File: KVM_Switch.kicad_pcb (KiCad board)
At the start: 4 copper layers, 100 x 70 mm, 110 parts, among them J1 HDMI_A, J2 HDMI_A, J3 HDMI_A, J4 USB_C_Receptacle_USB2.0_16P, J5 USB_C_Receptacle_USB2.0_16P, J6 USB_C_Receptacle_USB2.0_16P, J7 USB_A_Stacked, J8 USB_A_Stacked, SW1 SPST-NO, U1 TPD4E02B04DQA, U10 USBLC6-2SC6, U11 TS3USB221AQRSERQ1, U12 USBLC6-2SC6, U13 USB2514B_Bi, U14 USBLC6-2SC6, U15 USBLC6-2SC6, U16 USBLC6-2SC6, U17 USBLC6-2SC6, U2 TPD4E02B04DQA, U3 TPD4E02B04DQA, U4 TPD4E02B04DQA, U5 HD3SS215RTQR, U6 TPD4E02B04DQA, U7 TPD4E02B04DQA, U8 TLV75533PDBV, U9 STM32C031G6Ux, X1 24MHz

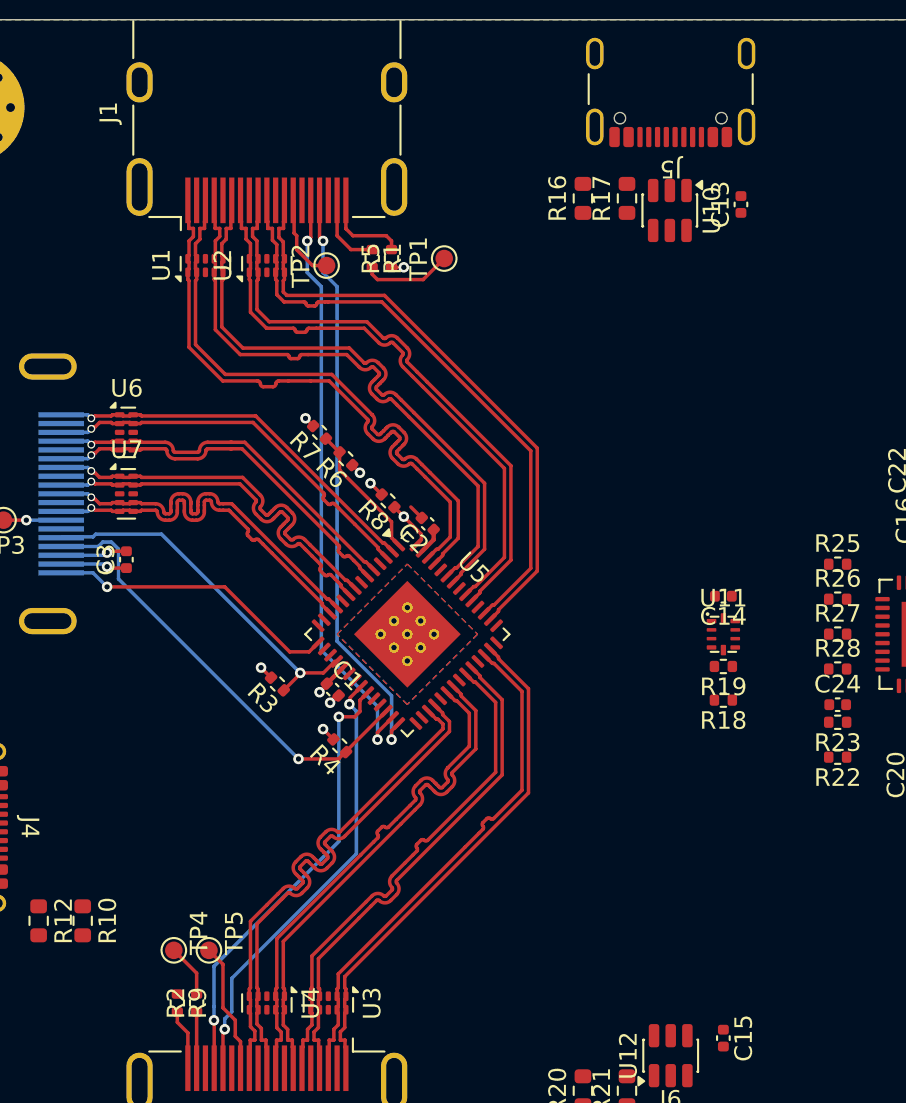
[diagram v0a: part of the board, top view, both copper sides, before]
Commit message: TMDS tunned to length
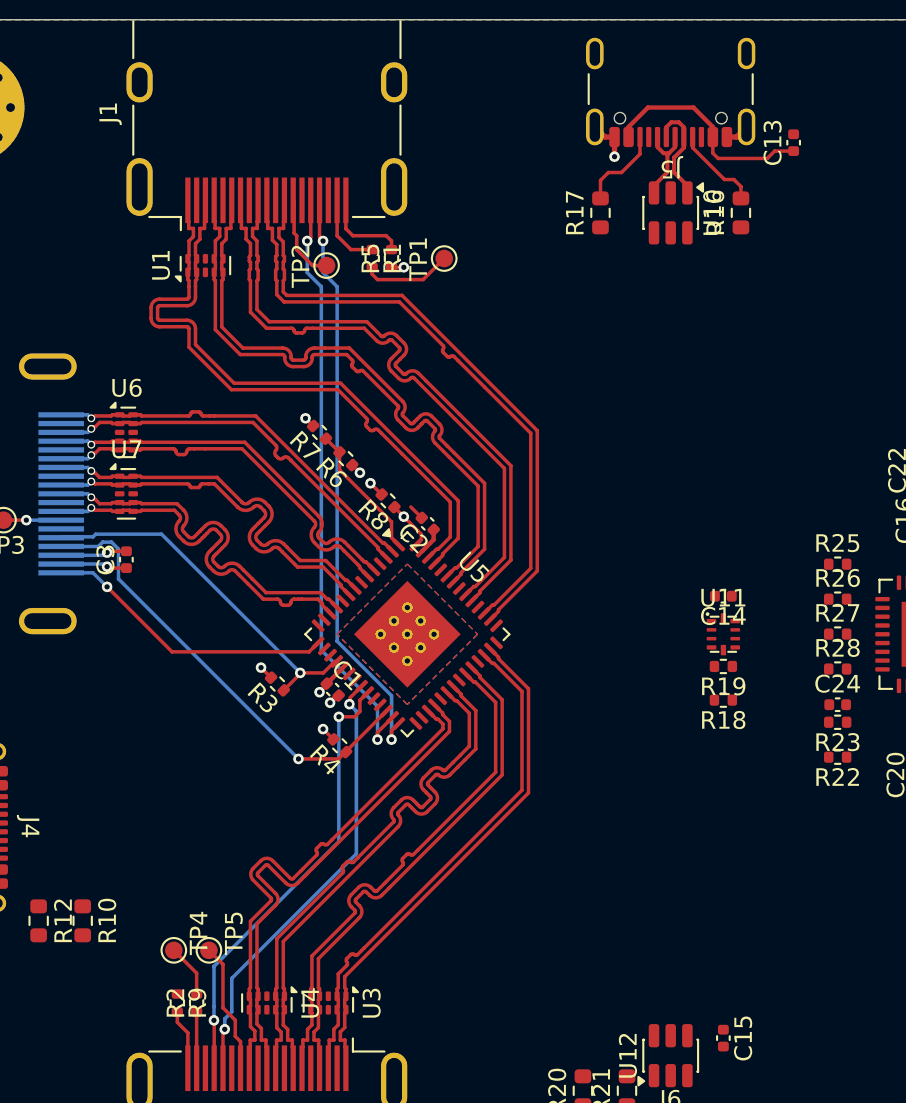
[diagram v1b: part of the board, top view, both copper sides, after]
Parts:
- removed U2: TPD4E02B04DQA, Package_SON:USON-10_2.5x1.0mm_P0.5mm
- moved R16 9.04 mm to (149.0, 76.0)
- moved C13 4.62 mm to (152.0, 72.0)
- moved R17 1.72 mm to (141.0, 76.0)
- moved U10 0.15 mm to (145.0, 76.0)
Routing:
- net /MCU/DET_USB_A: track 0.00 -> 12.7 mm
- net /USB_Host_Select/USB_CONN_A_DN: track 0.00 -> 6.08 mm
- net /USB_Host_Select/USB_CONN_A_DP: track 0.00 -> 5.05 mm
- net Net-(J5-CC1): track 0.00 -> 4.95 mm
- net Net-(J5-CC2): track 0.00 -> 4.87 mm
- net GND: track 7.65 -> 11.5 mm, vias 5 -> 6
- net /HDMI_Switch/HDMI_IN_A/D2_P: track 33.8 -> 35.2 mm
- net /HDMI_Switch/HDMI_IN_A/D2_N: track 33.9 -> 35.3 mm
- net /HDMI_Switch/HDMI_IN_A/D0_P: track 34.0 -> 35.2 mm
- net /HDMI_Switch/HDMI_IN_A/D0_N: track 34.1 -> 35.2 mm
- net /HDMI_Switch/HDMI_IN_B/D0_P: track 28.8 -> 29.7 mm
- net /HDMI_Switch/HDMI_IN_B/D0_N: track 28.8 -> 29.7 mm
- net /HDMI_Switch/HDMI_IN_A/D1_P: track 34.2 -> 35.0 mm
- net /HDMI_Switch/HDMI_IN_A/D1_N: track 34.2 -> 35.0 mm
- net /HDMI_Switch/HDMI_IN_A/CK_P: track 34.7 -> 35.3 mm
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
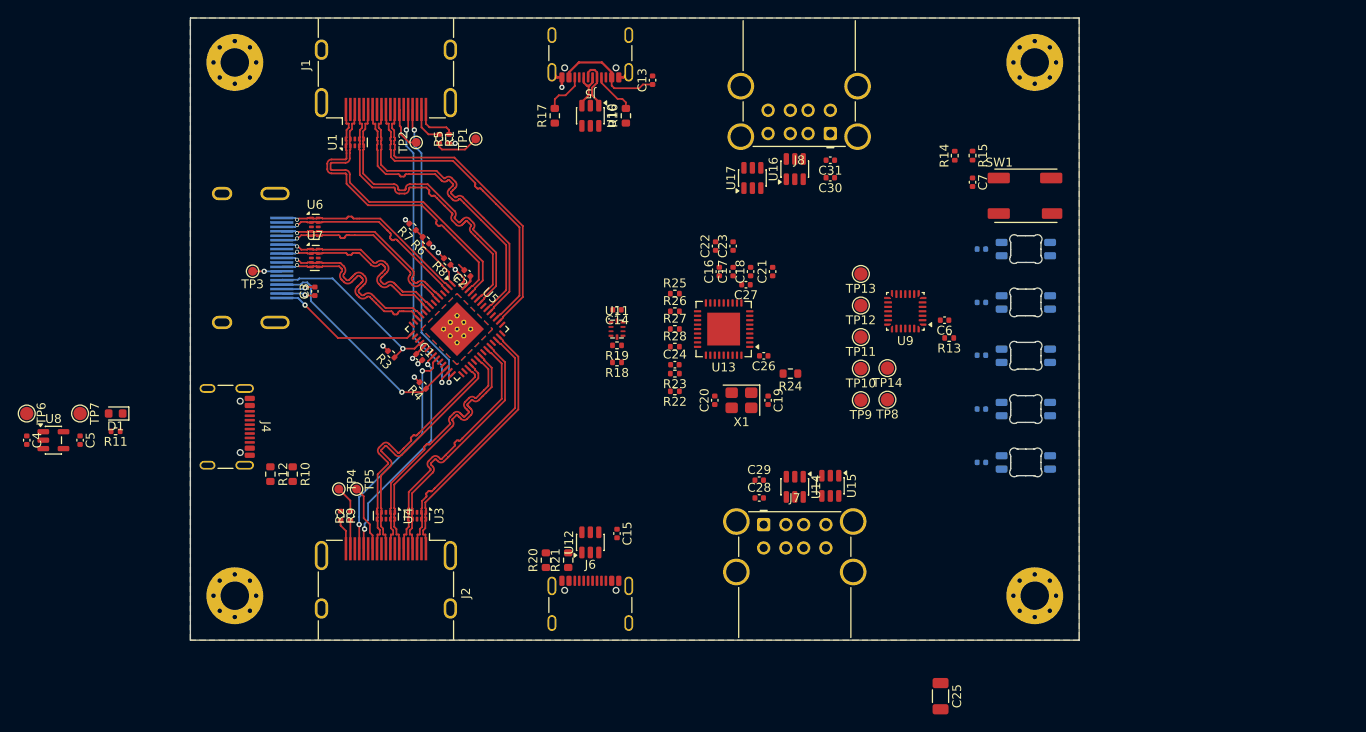
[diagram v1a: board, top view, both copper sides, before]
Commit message: Routed USB
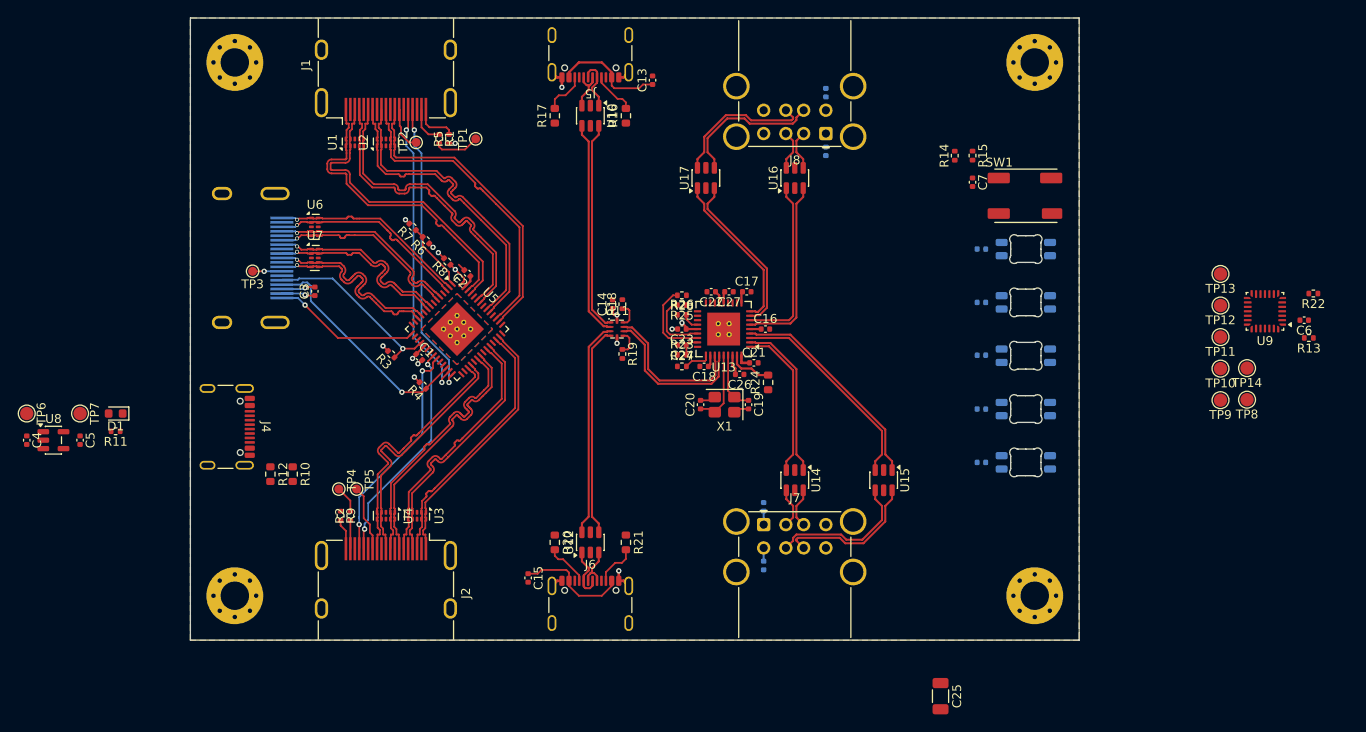
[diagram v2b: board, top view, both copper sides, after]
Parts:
- added U2: TPD4E02B04DQA, Package_SON:USON-10_2.5x1.0mm_P0.5mm, F.Cu at (122.0, 79.0)
- C28, C29, C30, C31: moved to B.Cu
- moved R22 72.7 mm to (226.3, 96.0)
- moved C6 40.5 mm to (225.3, 99.0)
- moved R13 40.5 mm to (225.8, 101.0)
- moved TP10 40.5 mm to (215.9, 104.5)
- moved TP11 40.5 mm to (215.9, 100.9)
- moved TP12 40.5 mm to (215.9, 97.3)
- moved TP13 40.5 mm to (215.9, 93.8)
- moved TP9 40.5 mm to (215.9, 108.0)
- moved U9 40.5 mm to (220.9, 98.0)
- moved TP14 40.5 mm to (218.9, 104.4)
- moved TP8 40.5 mm to (218.9, 107.9)
- moved C18 11.9 mm to (157.8, 104.2), turned to 180 degrees
- moved C15 11.2 mm to (138.0, 128.0)
- moved C23 11.0 mm to (155.3, 100.0), turned to 180 degrees
- moved C21 10.5 mm to (163.4, 103.8), turned to 0 degrees
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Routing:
- net /USB_Hub/USB_DOWN_1/USB2_DP: track 0.00 -> 24.6 mm
- net /USB_Host_Select/USB_B_DN: track 0.00 -> 24.4 mm
- net /USB_Host_Select/USB_A_DP: track 0.00 -> 24.4 mm
- net /USB_Hub/USB_DOWN_1/USB2_DN: track 0.00 -> 23.9 mm
- net /USB_Host_Select/USB_A_DN: track 0.00 -> 23.8 mm
- net /USB_Host_Select/USB_B_DP: track 0.00 -> 23.8 mm
- net /USB_Hub/USB_DOWN_2/USB1_DN: track 0.00 -> 20.5 mm
- net /USB_Hub/USB_DOWN_2/USB1_DP: track 0.00 -> 19.8 mm
- net /USB_Hub/USB_DOWN_2/USB2_DN: track 0.00 -> 18.8 mm
- net /USB_Hub/USB_DOWN_2/USB2_DP: track 0.00 -> 18.2 mm
- net /USB_Hub/USB_DOWN_1/USB1_DP: track 0.00 -> 18.2 mm
- net /USB_Host_Select/USB_UP_DP: track 0.00 -> 17.7 mm
- net /USB_Hub/USB_DOWN_1/USB1_DN: track 0.00 -> 17.6 mm
- net /USB_Host_Select/USB_UP_DN: track 0.00 -> 17.1 mm
- net /USB_Hub/USB_DOWN_1/USB2_CONN_DP: track 0.00 -> 16.5 mm
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
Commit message: USB matched lenght
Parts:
- moved TP10 14.6 mm to (228.1, 96.5)
- moved TP11 14.6 mm to (228.1, 92.9)
- moved TP13 5.54 mm to (214.0, 99.0)
- moved R22 4.80 mm to (222.6, 93.0)
- moved TP12 2.05 mm to (215.9, 95.3)
- moved C6 1.52 mm to (224.8, 97.5), turned to 90 degrees
- moved U9 0.99 mm to (221.6, 97.3)
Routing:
- net +3V3: track 15.2 -> 16.2 mm, vias 4 -> 5
- net /USB_Hub/USB_DOWN_2/USB1_DP: track 19.8 -> 20.4 mm
- net /USB_Host_Select/USB_UP_DN: track 17.1 -> 17.7 mm
- net /USB_Hub/USB_DOWN_1/USB2_DN: track 23.9 -> 24.5 mm
- net /USB_Host_Select/USB_A_DN: track 23.8 -> 24.3 mm
- net /USB_Host_Select/USB_B_DP: track 23.8 -> 24.3 mm
- net /USB_Hub/USB_DOWN_1/USB1_DN: track 17.6 -> 18.1 mm
- net GND: track 20.1 -> 20.0 mm, vias 9 -> 10

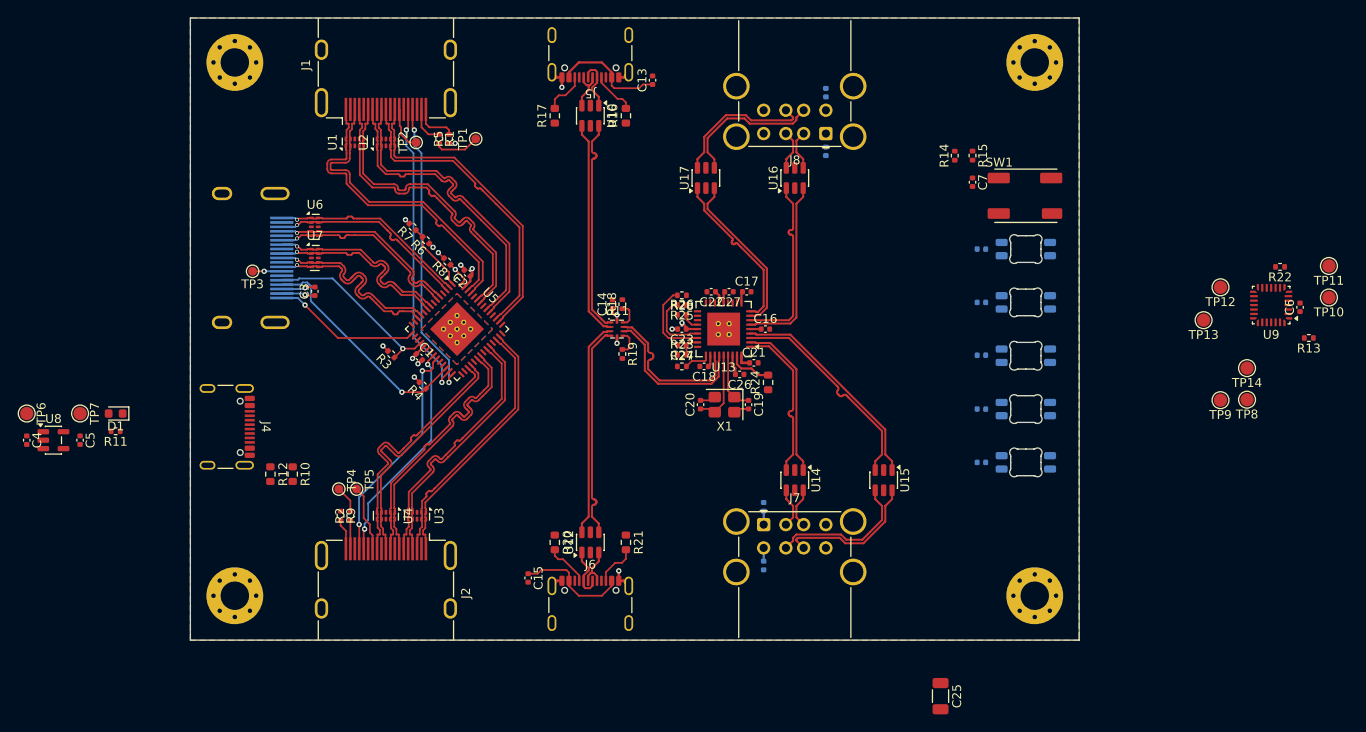
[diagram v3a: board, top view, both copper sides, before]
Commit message: Routed some low-speed tracks
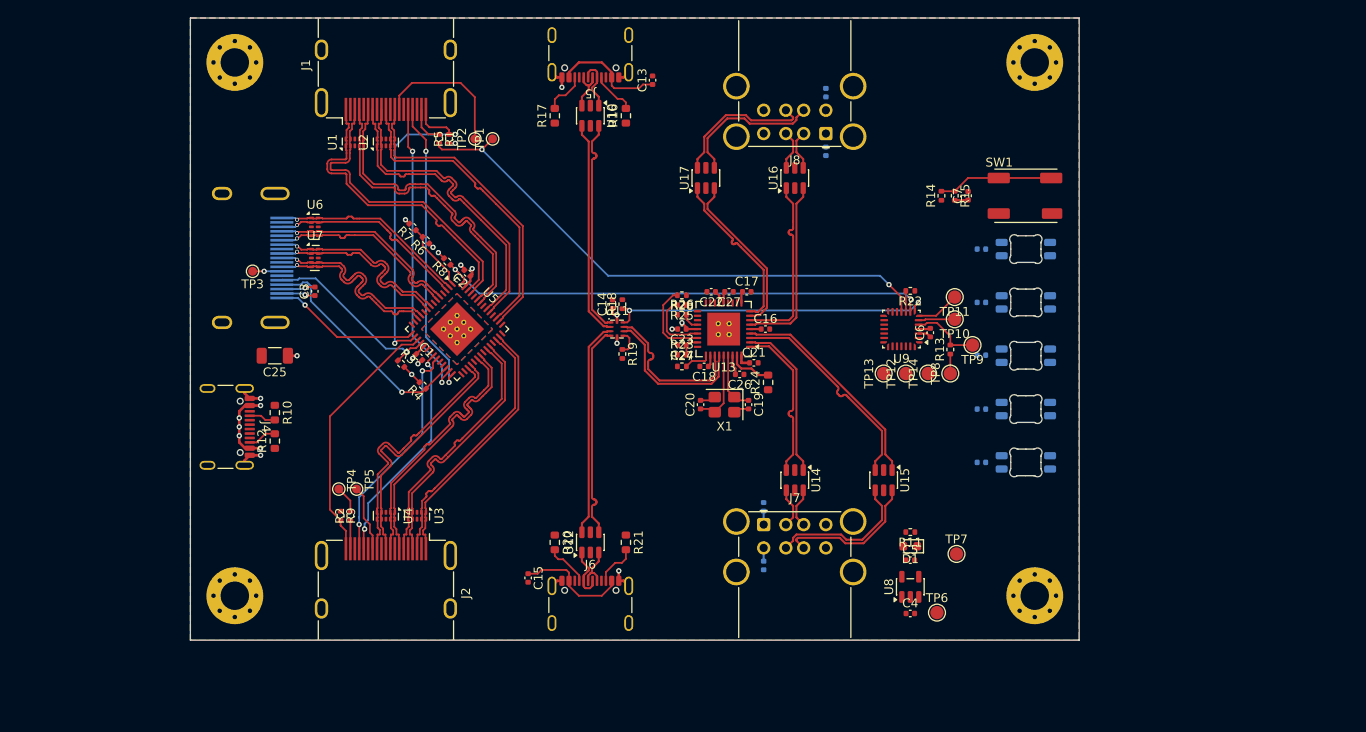
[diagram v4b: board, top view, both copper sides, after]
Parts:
- moved TP6 104.8 mm to (184.0, 131.9), turned to 0 degrees
- moved C4 101.3 mm to (181.0, 132.0), turned to 0 degrees
- moved TP7 99.9 mm to (186.2, 125.3), turned to 0 degrees
- moved U8 97.8 mm to (181.0, 129.0), turned to 90 degrees
- moved C5 94.4 mm to (181.0, 126.0), turned to 0 degrees
- moved D1 90.6 mm to (181.0, 124.4)
- moved R11 90.1 mm to (181.0, 122.8)
- moved C25 84.1 mm to (109.5, 103.0), turned to 180 degrees
- moved TP11 42.2 mm to (186.0, 96.4)
- moved TP10 42.2 mm to (186.0, 98.9)
- moved C6 41.7 mm to (183.2, 100.4)
- moved R22 41.7 mm to (181.0, 95.7)
- moved U9 41.7 mm to (180.0, 100.0)
- moved R13 40.4 mm to (185.5, 102.3), turned to 90 degrees
- moved TP12 36.7 mm to (180.5, 105.0), turned to 90 degrees
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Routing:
- net /HDMI_Switch/DET_A: track 5.11 -> 62.7 mm, vias 0 -> 2
- net /HDMI_Switch/SW: track 2.92 -> 57.0 mm, vias 1 -> 2
- net /MCU/USB_SW: track 2.81 -> 36.8 mm, vias 0 -> 2
- net /HDMI_Switch/HDMI_IN_A/HPD: track 4.99 -> 37.8 mm, vias 0 -> 2
- net /HDMI_Switch/HDMI_IN_B/HPD: track 3.45 -> 29.1 mm
- net Net-(R14-Pad2): track 0.00 -> 13.0 mm
- net /HDMI_Switch/HDMI_IN_A/CEC: track 4.97 -> 16.0 mm
- net VBUS: track 8.47 -> 19.4 mm, vias 3 -> 8
- net /MCU/RST: track 0.00 -> 7.76 mm
- net GND: track 20.0 -> 26.5 mm, vias 10 -> 12
- net /MCU/UART_RX: track 0.00 -> 4.87 mm
- net /MCU/UART_TX: track 0.00 -> 4.10 mm
- net +3V3: track 16.2 -> 19.8 mm
- net Net-(J4-CC2): track 0.00 -> 3.22 mm
- net Net-(J4-CC1): track 0.00 -> 3.02 mm
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
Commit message: Added series resistors for USB_DET & SW, HubOsc testpoints
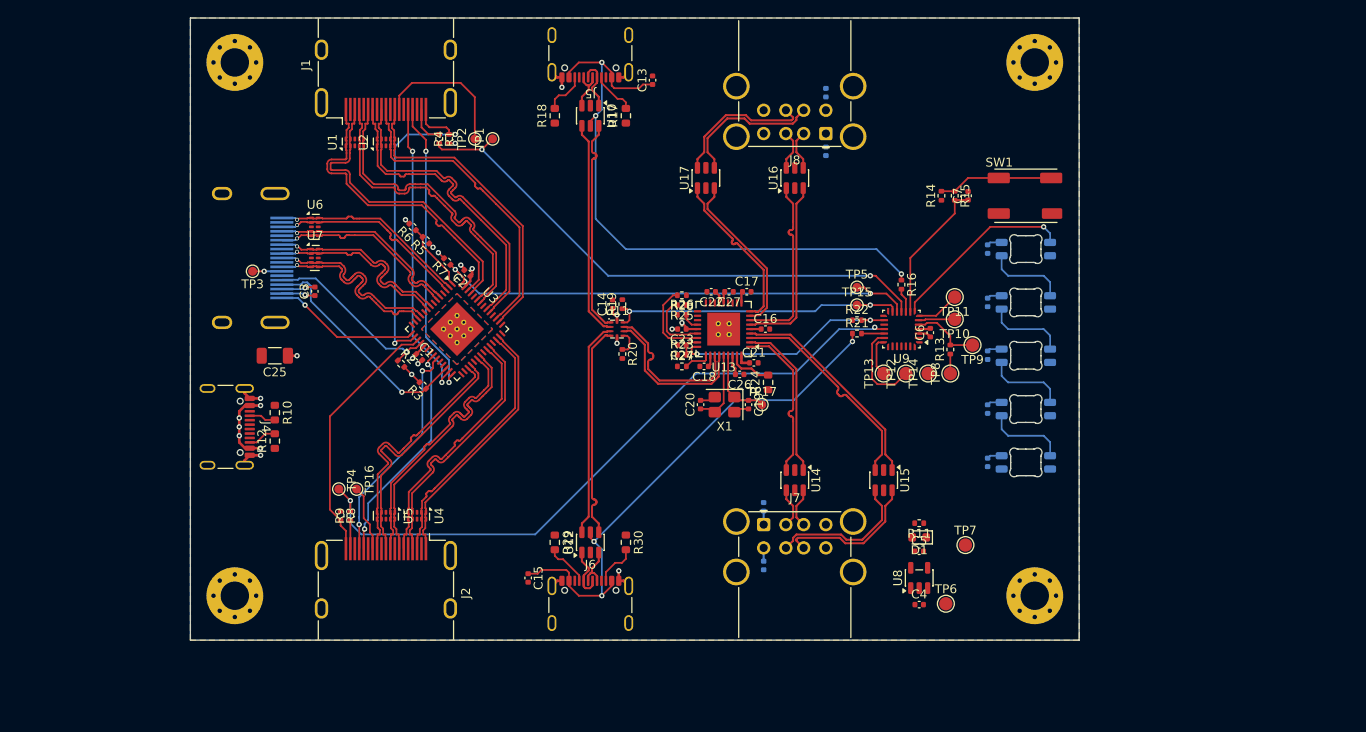
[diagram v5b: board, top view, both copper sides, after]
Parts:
- added R16: 10k, Resistor_SMD:R_0402_1005Metric, F.Cu at (180.0, 95.0)
- added R21: 10k, Resistor_SMD:R_0402_1005Metric, F.Cu at (175.0, 100.5)
- added TP15: TestPoint, TestPoint:TestPoint_Pad_D1.0mm, F.Cu at (175.0, 97.3)
- added TP17: TestPoint, TestPoint:TestPoint_Pad_D1.0mm, F.Cu at (164.3, 108.5)
- added TP5: TestPoint, TestPoint:TestPoint_Pad_D1.0mm, F.Cu at (175.0, 95.3)
- moved R22 6.85 mm to (175.0, 99.0), turned to 0 degrees
- moved C4 1.41 mm to (182.0, 131.0)
- moved C5 1.41 mm to (182.0, 125.0)
- moved D1 1.41 mm to (182.0, 123.4)
- moved R11 1.41 mm to (182.0, 121.8)
- moved TP6 1.41 mm to (185.0, 130.9)
- moved TP7 1.41 mm to (187.2, 124.3)
- moved U8 1.41 mm to (182.0, 128.0)
- moved C10 0.70 mm to (189.7, 102.9), turned to -90 degrees
- moved C11 0.70 mm to (189.7, 109.0), turned to -90 degrees
- moved C12 0.70 mm to (189.7, 115.0), turned to -90 degrees
- moved C8 0.70 mm to (189.7, 91.0), turned to -90 degrees
- moved C9 0.70 mm to (189.7, 97.0), turned to -90 degrees
- renumbered R16 to R17, R17 to R18, R18 to R19, R3 to R2, R19 to R20, R20 to R29, R4 to R3, R21 to R30, R5 to R4, R6 to R5, R7 to R6, R8 to R7, R9 to R8, R2 to R9, TP5 to TP16, U5 to U3, U3 to U4, U4 to U5
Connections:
- C13 pad 1: /MCU/DET_USB_A -> Net-(U10-VBUS)
- C15 pad 1: /MCU/DET_USB_B -> Net-(U12-VBUS)
- J5 pad A4: /MCU/DET_USB_A -> Net-(U10-VBUS)
- J5 pad A9: /MCU/DET_USB_A -> Net-(U10-VBUS)
- J5 pad B4: /MCU/DET_USB_A -> Net-(U10-VBUS)
- J5 pad B9: /MCU/DET_USB_A -> Net-(U10-VBUS)
- J6 pad A4: /MCU/DET_USB_B -> Net-(U12-VBUS)
- J6 pad A9: /MCU/DET_USB_B -> Net-(U12-VBUS)
- J6 pad B4: /MCU/DET_USB_B -> Net-(U12-VBUS)
- J6 pad B9: /MCU/DET_USB_B -> Net-(U12-VBUS)
- U10 pad 5: /MCU/DET_USB_A -> Net-(U10-VBUS)
- U12 pad 5: /MCU/DET_USB_B -> Net-(U12-VBUS)
- U9 pad 10: /MCU/UP_DET -> /MCU/DET_USB_A
- U9 pad 12: /HDMI_Switch/DET_B -> /HDMI_Switch/SW
- U9 pad 13: /MCU/LED -> /MCU/USB_SW
- U9 pad 14: /MCU/DET_USB_A -> unconnected-(U9-PB0-Pad14)
- U9 pad 15: /MCU/DET_USB_B -> unconnected-(U9-PB1-Pad15)
- U9 pad 16: /MCU/BTN -> /MCU/UP_DET
- U9 pad 18: unconnected-(U9-PA11-Pad18) -> /HDMI_Switch/DET_B
- U9 pad 19: unconnected-(U9-PA12-Pad19) -> /MCU/DET_USB_B
- U9 pad 8: /MCU/USB_SW -> /MCU/LED
- U9 pad 9: /HDMI_Switch/SW -> /MCU/BTN
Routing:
- net /HDMI_Switch/DET_B: track 3.03 -> 75.9 mm, vias 0 -> 2
- net Net-(U10-VBUS): track 0.00 -> 69.6 mm, vias 0 -> 3
- net Net-(U12-VBUS): track 0.00 -> 59.9 mm, vias 0 -> 3
- net /MCU/UP_DET: track 2.37 -> 26.6 mm, vias 0 -> 2
- net /MCU/LED: track 0.00 -> 21.1 mm, vias 0 -> 1
- net /MCU/BTN: track 1.51 -> 16.1 mm
- net /MCU/SWDIO: track 0.00 -> 10.1 mm
- net /MCU/DET_USB_B: track 12.7 -> 2.55 mm
- net /MCU/DET_USB_A: track 12.7 -> 2.76 mm
- net Net-(D2-DOUT): track 0.00 -> 9.10 mm
- net Net-(D5-DOUT): track 0.00 -> 9.10 mm
- net Net-(D4-DOUT): track 0.00 -> 9.10 mm
- net Net-(D3-DOUT): track 0.00 -> 9.10 mm
- net VBUS: track 19.4 -> 27.8 mm
- net /MCU/SWCLK: track 0.00 -> 4.52 mm
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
